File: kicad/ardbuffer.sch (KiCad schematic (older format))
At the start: 8 parts, among them P10 LCD, P11 SPI_EXP, P3 ARDUINO_MEGA_D, P8 ARDUINO_ADCH, P9 ARDUINO_COMM

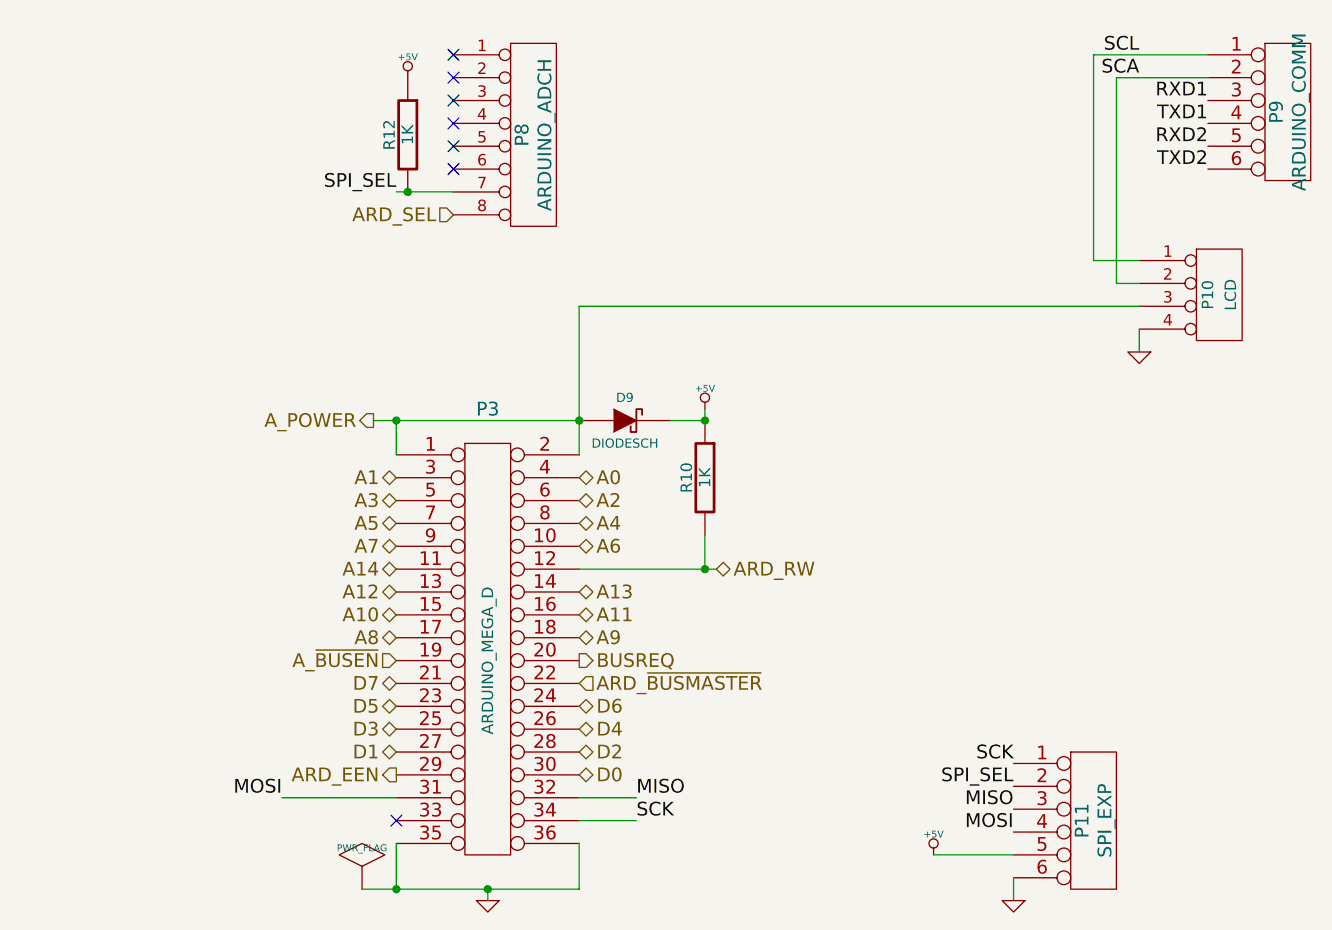
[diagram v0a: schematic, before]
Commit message: start of integration of common bus into CPLD
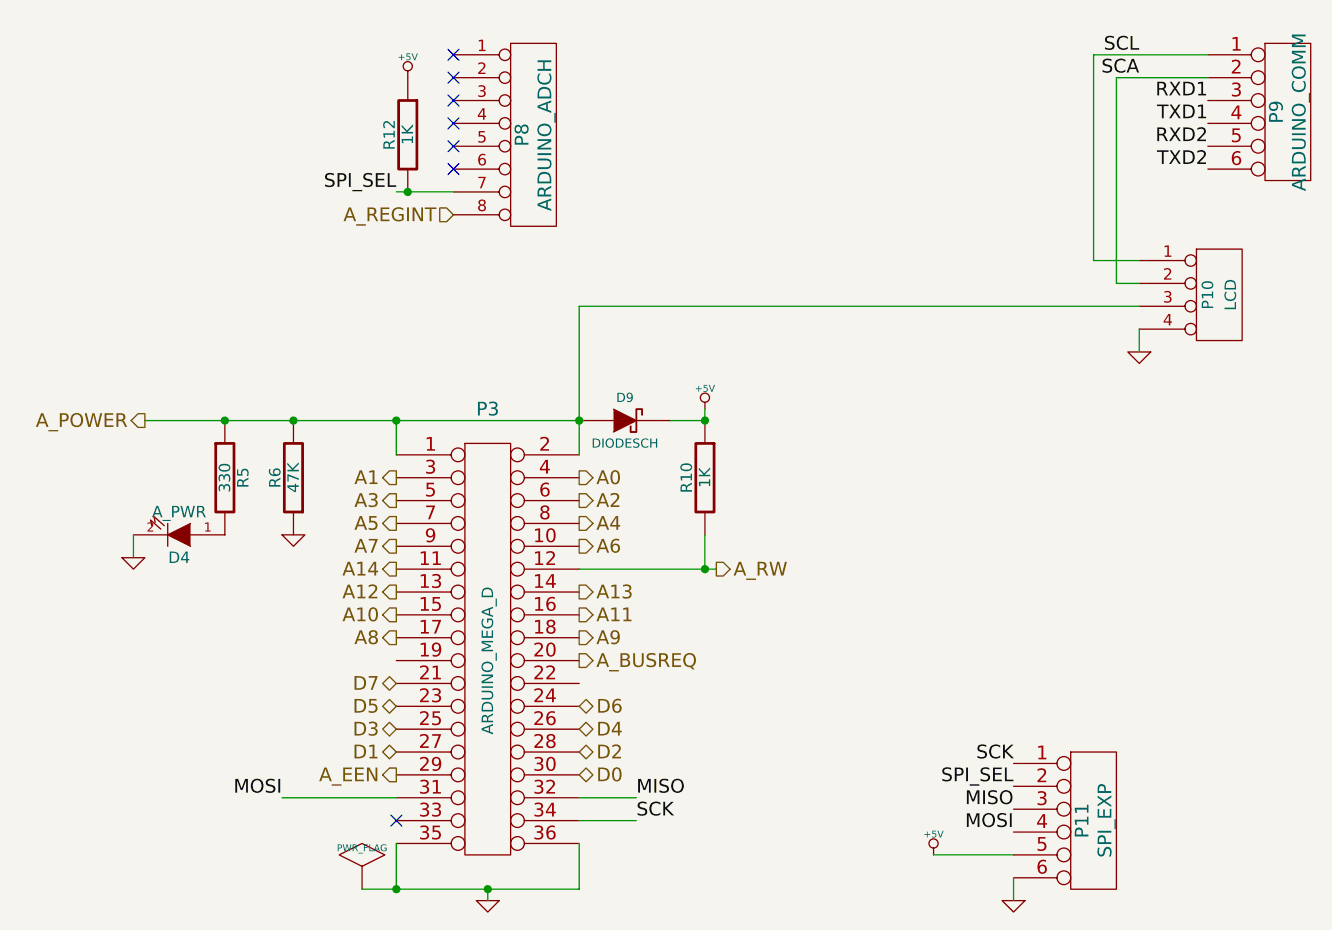
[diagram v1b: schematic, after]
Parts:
- added D4: A_PWR, symbol LED
- added R5: 330, symbol R
- added R6: 47K, symbol R
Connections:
- net A_POWER: now also R5.1, R6.2
- net GND: now also D4.2 (K), R6.1
- net ARD_EEN renamed A_EEN
- net ARD_RW renamed A_RW
- net ARD_SEL renamed A_REGINT
- net ARD_~BUSMASTER: no longer names the net of P3.22 (P22)
- net A_~BUSEN: no longer names the net of P3.19 (P19)
- net BUSREQ renamed A_BUSREQ
- new net: D4.1 (A), R5.2
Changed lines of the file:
@@
-EESchema Schematic File Version 2  date 4/22/2013 8:21:37 PM
+EESchema Schematic File Version 2  date 5/5/2013 11:17:22 AM
 LIBS:power
 LIBS:device
@@
 Sheet 2 3
 Title "Color Computer Bus Interface"
-Date "23 apr 2013"
-Rev "1.2"
-Comp "Bexkat Systems LLC"
+Date "5 may 2013"
+Rev "1.3"
+Comp "Bexkat Systems LLC 2013"
 Comment1 ""
 Comment2 ""
@@
 Comment4 ""
 $EndDescr
-$Comp
-L +5V #PWR022
+Wire Wire Line
+	1500 3700 1500 3800
+Wire Wire Line
+	5000 5100 5350 5100
+Wire Wire Line
+	5350 5200 5350 5300
+Wire Wire Line
+	6200 1600 5700 1600
+Wire Wire Line
+	5900 2500 5700 2500
+Wire Wire Line
+	5700 2500 5700 1600
+Wire Wire Line
+	5900 2700 3450 2700
+Wire Wire Line
+	3450 2700 3450 3350
+Wire Wire Line
+	3450 3850 4050 3850
+Connection ~ 4000 3200
+Wire Wire Line
+	3450 4950 3700 4950
+Wire Wire Line
+	2650 4850 2150 4850
+Connection ~ 3450 3200
+Wire Wire Line
+	2650 5250 2650 5050
+Wire Wire Line
+	2650 3200 2650 3350
+Wire Wire Line
+	3050 5250 3050 5300
+Wire Wire Line
+	3450 5050 3450 5250
+Connection ~ 3050 5250
+Wire Wire Line
+	3450 5250 2500 5250
+Connection ~ 2650 5250
+Connection ~ 2650 3200
+Wire Wire Line
+	3700 4850 3450 4850
+Wire Wire Line
+	4000 3150 4000 3200
+Wire Wire Line
+	4000 3200 3850 3200
+Wire Wire Line
+	4000 3850 4000 3700
+Connection ~ 4000 3850
+Wire Wire Line
+	5900 2900 5900 2800
+Wire Wire Line
+	5900 2600 5800 2600
+Wire Wire Line
+	5800 2600 5800 1700
+Wire Wire Line
+	5800 1700 6200 1700
+Wire Wire Line
+	2650 2200 2900 2200
+Connection ~ 2700 2200
+Connection ~ 2200 3200
+Wire Wire Line
+	3450 3200 1550 3200
+Connection ~ 1900 3200
+$Comp
+L GND #PWR013
+U 1 1 517C60C1
+P 1500 3800
+F 0 "#PWR013" H 1500 3800 30  0001 C CNN
+F 1 "GND" H 1500 3730 30  0001 C CNN
+	1    1500 3800
+	1    0    0    -1
+$EndComp
+$Comp
+L LED D4
+U 1 1 517C6089
+P 1700 3700
+F 0 "D4" H 1700 3800 50  0000 C CNN
+F 1 "A_PWR" H 1700 3600 50  0000 C CNN
+	1    1700 3700
+	-1   0    0    1
+$EndComp
+$Comp
+L R R5
+U 1 1 517C6087
+P 1900 3450
+F 0 "R5" V 1980 3450 50  0000 C CNN
+F 1 "330" V 1900 3450 50  0000 C CNN
+	1    1900 3450
+	1    0    0    -1
+$EndComp
+$Comp
+L GND #PWR014
+U 1 1 517C547C
+P 2200 3700
+F 0 "#PWR014" H 2200 3700 30  0001 C CNN
+F 1 "GND" H 2200 3630 30  0001 C CNN
+	1    2200 3700
+	1    0    0    -1
+$EndComp
+$Comp
+L R R6
+U 1 1 517C5468
+P 2200 3450
+F 0 "R6" V 2280 3450 50  0000 C CNN
+F 1 "47K" V 2200 3450 50  0000 C CNN
+	1    2200 3450
+	-1   0    0    1
+$EndComp
+$Comp
+L +5V #PWR015
 U 1 1 5175D31E
 P 2700 1700
-F 0 "#PWR022" H 2700 1790 20  0001 C CNN
+F 0 "#PWR015" H 2700 1790 20  0001 C CNN
 F 1 "+5V" H 2700 1790 30  0000 C CNN
 	1    2700 1700
 	-1   0    0    -1
 $EndComp
-Connection ~ 2700 2200
 $Comp
 L R R12
@@
 	-1   0    0    -1
 $EndComp
-Wire Wire Line
-	2650 2200 2900 2200
-Wire Wire Line
-	6200 1700 5800 1700
-Wire Wire Line
-	5800 1700 5800 2600
-Wire Wire Line
-	5800 2600 5900 2600
-Wire Wire Line
-	5900 2900 5900 2800
-Connection ~ 4000 3850
-Wire Wire Line
-	4000 3850 4000 3700
-Wire Wire Line
-	3850 3200 4000 3200
-Wire Wire Line
-	4000 3200 4000 3150
-Wire Wire Line
-	3700 4850 3450 4850
-Connection ~ 2650 3200
-Connection ~ 2650 5250
-Wire Wire Line
-	2500 5250 3450 5250
-Connection ~ 3050 5250
-Wire Wire Line
-	3450 5250 3450 5050
-Wire Wire Line
-	3050 5250 3050 5300
-Wire Wire Line
-	2650 3200 2650 3350
-Wire Wire Line
-	2650 5250 2650 5050
-Wire Wire Line
-	3450 3200 2550 3200
-Connection ~ 3450 3200
-Wire Wire Line
-	2650 4850 2150 4850
-Wire Wire Line
-	3450 4950 3700 4950
-Connection ~ 4000 3200
-Wire Wire Line
-	3450 3850 4050 3850
-Wire Wire Line
-	3450 3350 3450 2700
-Wire Wire Line
-	3450 2700 5900 2700
-Wire Wire Line
-	5700 2500 5700 1600
-Wire Wire Line
-	5700 2500 5900 2500
-Wire Wire Line
-	5700 1600 6200 1600
-Wire Wire Line
-	5350 5200 5350 5300
-Wire Wire Line
-	5000 5100 5350 5100
 Text Label 5350 4700 2    60   ~ 0
 SCK
@@
 SPI_SEL
 $Comp
-L +5V #PWR023
+L +5V #PWR016
 U 1 1 5175D2AF
 P 5000 5100
-F 0 "#PWR023" H 5000 5190 20  0001 C CNN
+F 0 "#PWR016" H 5000 5190 20  0001 C CNN
 F 1 "+5V" H 5000 5190 30  0000 C CNN
 	1    5000 5100
@@
 $EndComp
 $Comp
-L GND #PWR024
+L GND #PWR017
 U 1 1 5175D2A4
 P 5350 5300
-F 0 "#PWR024" H 5350 5300 30  0001 C CNN
+F 0 "#PWR017" H 5350 5300 30  0001 C CNN
 F 1 "GND" H 5350 5230 30  0001 C CNN
 	1    5350 5300
@@
 Text Label 6200 1800 2    60   ~ 0
 RXD1
-Text HLabel 3450 4350 2    60   Input ~ 0
-ARD_~BUSMASTER
-$Comp
-L GND #PWR025
+$Comp
+L GND #PWR018
 U 1 1 5174ADB7
 P 5900 2900
-F 0 "#PWR025" H 5900 2900 30  0001 C CNN
+F 0 "#PWR018" H 5900 2900 30  0001 C CNN
 F 1 "GND" H 5900 2830 30  0001 C CNN
 	1    5900 2900
@@
 $EndComp
 Text HLabel 2900 2300 0    60   Input ~ 0
-ARD_SEL
+A_REGINT
 Text HLabel 2650 4750 0    60   Output ~ 0
-ARD_EEN
-$Comp
-L +5V #PWR026
+A_EEN
+$Comp
+L +5V #PWR019
 U 1 1 516FEC4E
 P 4000 3150
-F 0 "#PWR026" H 4000 3240 20  0001 C CNN
+F 0 "#PWR019" H 4000 3240 20  0001 C CNN
 F 1 "+5V" H 4000 3240 30  0000 C CNN
 	1    4000 3150
@@
 $EndComp
 $Comp
-L PWR_FLAG #FLG027
+L PWR_FLAG #FLG020
 U 1 1 5158EE04
 P 2500 5250
-F 0 "#FLG027" H 2500 5345 30  0001 C CNN
+F 0 "#FLG020" H 2500 5345 30  0001 C CNN
 F 1 "PWR_FLAG" H 2500 5430 30  0000 C CNN
 	1    2500 5250
 	1    0    0    -1
 $EndComp
-Text HLabel 2550 3200 0    60   Output ~ 0
+Text HLabel 1550 3200 0    60   Output ~ 0
 A_POWER
-Text HLabel 4050 3850 2    60   BiDi ~ 0
-ARD_RW
+Text HLabel 4050 3850 2    60   Output ~ 0
+A_RW
 Text HLabel 3450 4250 2    60   Output ~ 0
-BUSREQ
-Text HLabel 3450 3950 2    60   BiDi ~ 0
+A_BUSREQ
+Text HLabel 3450 3950 2    60   Output ~ 0
 A13
-Text HLabel 2650 3850 0    60   BiDi ~ 0
+Text HLabel 2650 3850 0    60   Output ~ 0
 A14
-Text HLabel 2650 3950 0    60   BiDi ~ 0
+Text HLabel 2650 3950 0    60   Output ~ 0
 A12
-Text HLabel 3450 4050 2    60   BiDi ~ 0
+Text HLabel 3450 4050 2    60   Output ~ 0
 A11
-Text HLabel 2650 4050 0    60   BiDi ~ 0
+Text HLabel 2650 4050 0    60   Output ~ 0
 A10
-Text HLabel 3450 4150 2    60   BiDi ~ 0
+Text HLabel 3450 4150 2    60   Output ~ 0
 A9
-Text HLabel 2650 4150 0    60   BiDi ~ 0
+Text HLabel 2650 4150 0    60   Output ~ 0
 A8
-Text HLabel 2650 3750 0    60   BiDi ~ 0
+Text HLabel 2650 3750 0    60   Output ~ 0
 A7
-Text HLabel 3450 3750 2    60   BiDi ~ 0
+Text HLabel 3450 3750 2    60   Output ~ 0
 A6
-Text HLabel 2650 3650 0    60   BiDi ~ 0
+Text HLabel 2650 3650 0    60   Output ~ 0
 A5
-Text HLabel 3450 3650 2    60   BiDi ~ 0
+Text HLabel 3450 3650 2    60   Output ~ 0
 A4
-Text HLabel 2650 3550 0    60   BiDi ~ 0
+Text HLabel 2650 3550 0    60   Output ~ 0
 A3
-Text HLabel 3450 3550 2    60   BiDi ~ 0
+Text HLabel 3450 3550 2    60   Output ~ 0
 A2
-Text HLabel 2650 3450 0    60   BiDi ~ 0
+Text HLabel 2650 3450 0    60   Output ~ 0
 A1
-Text HLabel 3450 3450 2    60   BiDi ~ 0
+Text HLabel 3450 3450 2    60   Output ~ 0
 A0
 Text HLabel 2650 4350 0    60   BiDi ~ 0
@@
 Text HLabel 3450 4750 2    60   BiDi ~ 0
 D0
-Text HLabel 2650 4250 0    60   Input ~ 0
-A_~BUSEN
 $Comp
 L CONN_18X2 P3
@@
 $EndComp
 $Comp
-L GND #PWR028
+L GND #PWR021
 U 1 1 5156E4FE
 P 3050 5300
-F 0 "#PWR028" H 3050 5300 30  0001 C CNN
+F 0 "#PWR021" H 3050 5300 30  0001 C CNN
 F 1 "GND" H 3050 5230 30  0001 C CNN
 	1    3050 5300

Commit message: implement control logic for register memory
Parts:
- R5: value 330 -> 150
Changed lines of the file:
@@
-EESchema Schematic File Version 2  date 5/5/2013 11:17:22 AM
+EESchema Schematic File Version 2  date Tue 07 May 2013 02:44:39 PM EDT
 LIBS:power
 LIBS:device
@@
 Sheet 2 3
 Title "Color Computer Bus Interface"
-Date "5 may 2013"
+Date "7 may 2013"
 Rev "1.3"
 Comp "Bexkat Systems LLC 2013"
@@
 P 1900 3450
 F 0 "R5" V 1980 3450 50  0000 C CNN
-F 1 "330" V 1900 3450 50  0000 C CNN
+F 1 "150" V 1900 3450 50  0000 C CNN
 	1    1900 3450
 	1    0    0    -1
